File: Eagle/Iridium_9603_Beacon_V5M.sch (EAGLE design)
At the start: 104 parts, among them CON4 uFL, J1 SS4-10-3.50-X-D, Q1 DMG3415U-7, Q2 DMG3415U-7, Q3 DMG3415U-7, Q4 DMG3415U-7, Q5 2N2222, U1 MCP111T-240E/TT, U2 SPX3819-3.3, U3 LTC3225EDDB#TRMPBF, U4 MPL3115A2LGA8, U5 ATSAMD21G18_QFN, U53 7101K2AV2QE, U6 MAX-M8, U7 LT1634-1,25BMCMS8, X1 32.768

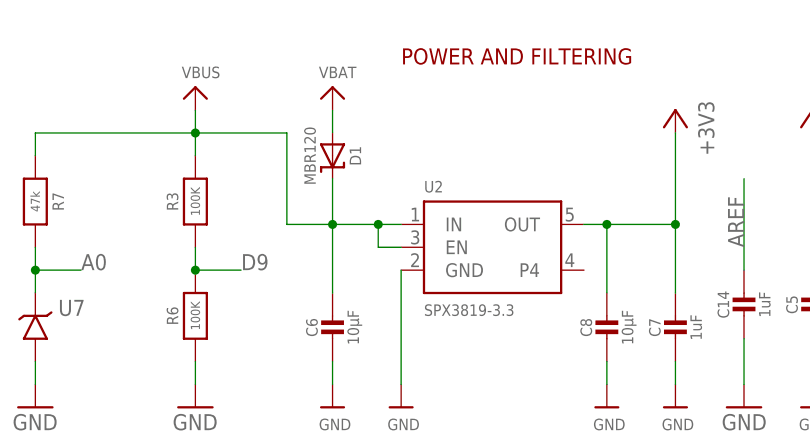
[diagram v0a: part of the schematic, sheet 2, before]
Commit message: Added diode to second battery pack
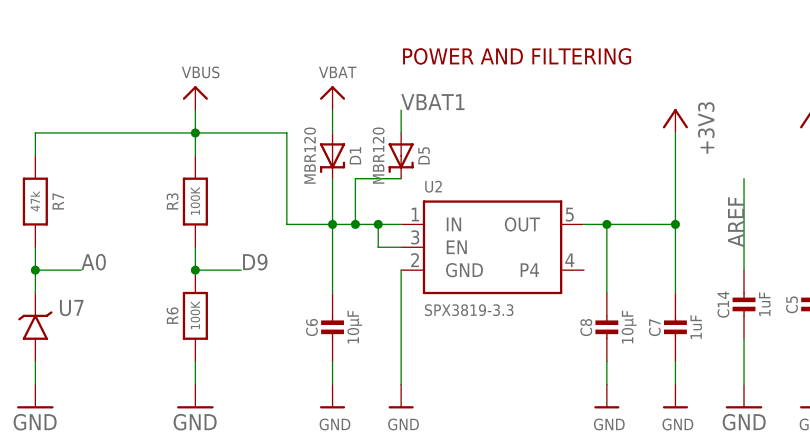
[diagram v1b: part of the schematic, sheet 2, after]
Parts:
- added D5: MBR120, microbuilder:DIODE-SCHOTTKYSOD-123
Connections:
- new net VBAT1: BAT4.+, D5.A
- net VBAT: no longer BAT4.+
- net VBUS: now also D5.C
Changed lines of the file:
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@@
 <part name="GND6" library="adafruit" library_urn="urn:adsk.eagle:library:420" deviceset="PINHD-1X1" device="" package3d_urn="urn:adsk.eagle:package:6240654/1"/>
 <part name="GND14" library="supply1" library_urn="urn:adsk.eagle:library:371" deviceset="GND" device=""/>
+<part name="D5" library="microbuilder" deviceset="DIODE-SCHOTTKY" device="SOD-123" value="MBR120"/>
 </parts>
 <sheets>
@@
 <wire x1="218.44" y1="111.76" x2="218.44" y2="114.3" width="0.1524" layer="91"/>
 <pinref part="BAT1" gate="G$1" pin="+"/>
-<pinref part="BAT4" gate="G$1" pin="+"/>
-<wire x1="218.44" y1="111.76" x2="236.22" y2="111.76" width="0.1524" layer="91"/>
-<junction x="218.44" y="111.76"/>
 </segment>
 </net>
@@
 <pinref part="BAT6" gate="G$1" pin="+"/>
 <wire x1="236.22" y1="88.9" x2="236.22" y2="86.36" width="0.1524" layer="91"/>
+</segment>
+</net>
+<net name="VBAT1" class="0">
+<segment>
+<pinref part="BAT4" gate="G$1" pin="+"/>
+<wire x1="236.22" y1="111.76" x2="236.22" y2="114.3" width="0.1524" layer="91"/>
+<label x="236.22" y="114.3" size="1.778" layer="95"/>
 </segment>
 </net>
@@
 <attribute name="VALUE" x="147.32" y="88.9" size="1.778" layer="96"/>
 </instance>
+<instance part="D5" gate="G$1" x="53.34" y="160.02" smashed="yes" rot="R270">
+<attribute name="NAME" x="55.88" y="160.02" size="1.27" layer="95" rot="R270" align="center"/>
+<attribute name="VALUE" x="50.84" y="160.02" size="1.27" layer="96" rot="R270" align="center"/>
+</instance>
 </instances>
 <busses>
@@
 <pinref part="C6" gate="G$1" pin="1"/>
 <wire x1="53.34" y1="152.4" x2="50.8" y2="152.4" width="0.1524" layer="91"/>
-<wire x1="50.8" y1="152.4" x2="45.72" y2="152.4" width="0.1524" layer="91"/>
+<wire x1="50.8" y1="152.4" x2="48.26" y2="152.4" width="0.1524" layer="91"/>
+<wire x1="48.26" y1="152.4" x2="45.72" y2="152.4" width="0.1524" layer="91"/>
 <wire x1="45.72" y1="152.4" x2="45.72" y2="144.78" width="0.1524" layer="91"/>
 <wire x1="45.72" y1="157.48" x2="45.72" y2="152.4" width="0.1524" layer="91"/>
@@
 <wire x1="12.7" y1="162.56" x2="12.7" y2="160.02" width="0.1524" layer="91"/>
 <pinref part="R3" gate="G$1" pin="2"/>
+<pinref part="D5" gate="G$1" pin="C"/>
+<wire x1="53.34" y1="157.48" x2="48.26" y2="157.48" width="0.1524" layer="91"/>
+<wire x1="48.26" y1="157.48" x2="48.26" y2="152.4" width="0.1524" layer="91"/>
+<junction x="48.26" y="152.4"/>
 </segment>
 <segment>
@@
 </segment>
 </net>
+<net name="VBAT1" class="0">
+<segment>
+<pinref part="D5" gate="G$1" pin="A"/>
+<wire x1="53.34" y1="162.56" x2="53.34" y2="165.1" width="0.1524" layer="91"/>
+<label x="53.34" y="165.1" size="1.778" layer="95"/>
+</segment>
+</net>
